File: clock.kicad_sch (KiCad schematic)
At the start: 10 parts

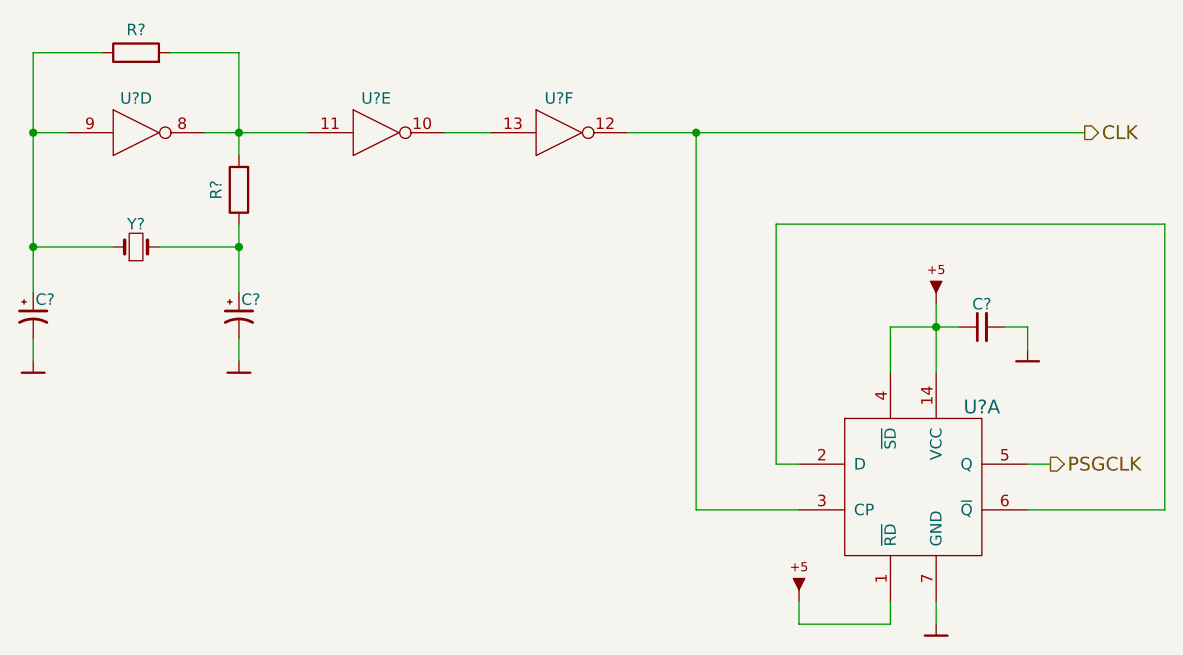
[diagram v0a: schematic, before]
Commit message: Fix wrong cap type in clock generator
Also fill some references automatically generated by KiCAD.
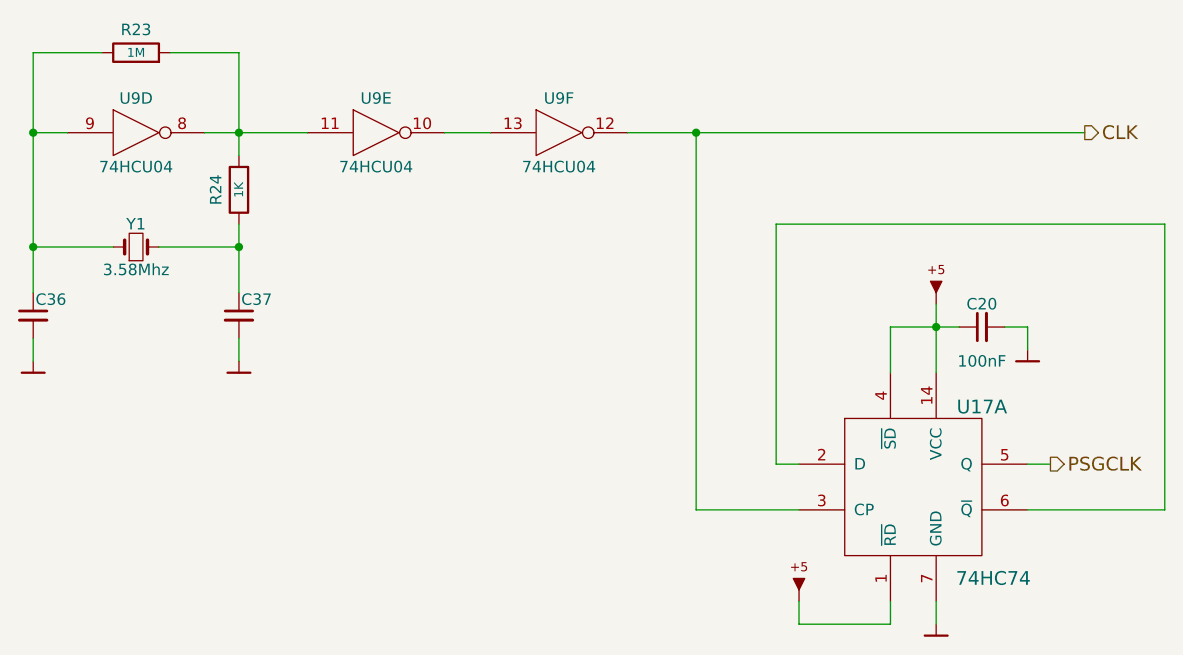
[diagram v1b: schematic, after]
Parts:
- C20: renamed from C?; value (none) -> 100nF; footprint (none) -> artemisa:Disc_capacitor
- C36, C37: renamed from C?; symbol artemisa:CP -> artemisa:Cap
- R23: renamed from R?; value (none) -> 1M; footprint (none) -> artemisa:Axial_resistor
- R24: renamed from R?; value (none) -> 1K; footprint (none) -> artemisa:Axial_resistor
- U17: renamed from U?; value (none) -> 74HC74; footprint (none) -> artemisa:DIP-14_300
- U9: renamed from U?; value (none) -> 74HCU04; footprint (none) -> artemisa:DIP-14_300
- Y1: renamed from Y?; value (none) -> 3.58Mhz; footprint (none) -> artemisa:Crystal
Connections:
- net VCC: now reaches U17.1 (~{RD})
- net VCC: now also C20.1, U17.14 (VCC), U17.4 (~{SD})
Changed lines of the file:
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@@
   (symbol (lib_id "artemisa:Crystal") (at 85.09 87.63 0) (unit 1)
     (in_bom yes) (on_board yes)
-    (property "Reference" "Y?" (id 0) (at 85.09 85.09 0))
-    (property "Value" "" (id 1) (at 85.09 90.17 0))
-    (property "Footprint" "" (id 2) (at 85.09 87.63 0)
+    (property "Reference" "Y1" (id 0) (at 85.09 85.09 0))
+    (property "Value" "3.58Mhz" (id 1) (at 85.09 90.17 0))
+    (property "Footprint" "artemisa:Crystal" (id 2) (at 85.09 87.63 0)
       (effects (font (size 1.27 1.27)) hide)
     )
@@
     (pin "2")
   )
-  (symbol (lib_id "artemisa:CP") (at 73.66 95.25 0) (unit 1)
-    (in_bom yes) (on_board yes)
-    (property "Reference" "C?" (id 0) (at 73.914 93.472 0)
+  (symbol (lib_id "artemisa:Cap") (at 73.66 95.25 0) (unit 1)
+    (in_bom yes) (on_board yes)
+    (property "Reference" "C36" (id 0) (at 73.914 93.472 0)
       (effects (font (size 1.27 1.27)) (justify left))
     )
@@
     (pin "2")
   )
-  (symbol (lib_id "artemisa:CP") (at 96.52 95.25 0) (unit 1)
-    (in_bom yes) (on_board yes)
-    (property "Reference" "C?" (id 0) (at 96.774 93.472 0)
+  (symbol (lib_id "artemisa:Cap") (at 96.52 95.25 0) (unit 1)
+    (in_bom yes) (on_board yes)
+    (property "Reference" "C37" (id 0) (at 96.774 93.472 0)
       (effects (font (size 1.27 1.27)) (justify left))
     )
@@
   (symbol (lib_id "artemisa:74HCU04") (at 85.09 74.93 0) (unit 4)
     (in_bom yes) (on_board yes)
-    (property "Reference" "U?" (id 0) (at 85.09 71.12 0))
-    (property "Value" "" (id 1) (at 85.09 78.74 0))
-    (property "Footprint" "" (id 2) (at 85.09 74.93 0)
+    (property "Reference" "U9" (id 0) (at 85.09 71.12 0))
+    (property "Value" "74HCU04" (id 1) (at 85.09 78.74 0))
+    (property "Footprint" "artemisa:DIP-14_300" (id 2) (at 85.09 74.93 0)
       (effects (font (size 1.27 1.27)) hide)
     )
@@
   (symbol (lib_id "artemisa:74HCU04") (at 111.76 74.93 0) (unit 5)
     (in_bom yes) (on_board yes)
-    (property "Reference" "U?" (id 0) (at 111.76 71.12 0))
-    (property "Value" "" (id 1) (at 111.76 78.74 0))
-    (property "Footprint" "" (id 2) (at 111.76 74.93 0)
+    (property "Reference" "U9" (id 0) (at 111.76 71.12 0))
+    (property "Value" "74HCU04" (id 1) (at 111.76 78.74 0))
+    (property "Footprint" "artemisa:DIP-14_300" (id 2) (at 111.76 74.93 0)
       (effects (font (size 1.27 1.27)) hide)
     )
@@
   (symbol (lib_id "artemisa:R") (at 96.52 81.28 90) (unit 1)
     (in_bom yes) (on_board yes)
-    (property "Reference" "R?" (id 0) (at 93.98 81.28 0))
-    (property "Value" "" (id 1) (at 96.52 81.28 0)
+    (property "Reference" "R24" (id 0) (at 93.98 81.28 0))
+    (property "Value" "1K" (id 1) (at 96.52 81.28 0)
       (effects (font (size 0.9906 0.9906)))
     )
-    (property "Footprint" "" (id 2) (at 96.52 83.058 90)
+    (property "Footprint" "artemisa:Axial_resistor" (id 2) (at 96.52 83.058 90)
       (effects (font (size 1.27 1.27)) hide)
     )
@@
   (symbol (lib_id "artemisa:R") (at 85.09 66.04 0) (unit 1)
     (in_bom yes) (on_board yes)
-    (property "Reference" "R?" (id 0) (at 85.09 63.5 0))
-    (property "Value" "" (id 1) (at 85.09 66.04 0)
+    (property "Reference" "R23" (id 0) (at 85.09 63.5 0))
+    (property "Value" "1M" (id 1) (at 85.09 66.04 0)
       (effects (font (size 0.9906 0.9906)))
     )
-    (property "Footprint" "" (id 2) (at 83.312 66.04 90)
+    (property "Footprint" "artemisa:Axial_resistor" (id 2) (at 83.312 66.04 90)
       (effects (font (size 1.27 1.27)) hide)
     )
@@
   (symbol (lib_id "artemisa:74HCU04") (at 132.08 74.93 0) (unit 6)
     (in_bom yes) (on_board yes)
-    (property "Reference" "U?" (id 0) (at 132.08 71.12 0))
-    (property "Value" "" (id 1) (at 132.08 78.74 0))
-    (property "Footprint" "" (id 2) (at 132.08 74.93 0)
+    (property "Reference" "U9" (id 0) (at 132.08 71.12 0))
+    (property "Value" "74HCU04" (id 1) (at 132.08 78.74 0))
+    (property "Footprint" "artemisa:DIP-14_300" (id 2) (at 132.08 74.93 0)
       (effects (font (size 1.27 1.27)) hide)
     )
@@
   (symbol (lib_id "artemisa:74HC74") (at 171.45 114.3 0) (unit 1)
     (in_bom yes) (on_board yes)
-    (property "Reference" "U?" (id 0) (at 179.07 105.41 0)
+    (property "Reference" "U17" (id 0) (at 179.07 105.41 0)
       (effects (font (size 1.524 1.524)))
     )
-    (property "Value" "" (id 1) (at 180.34 124.46 0)
+    (property "Value" "74HC74" (id 1) (at 180.34 124.46 0)
       (effects (font (size 1.524 1.524)))
     )
-    (property "Footprint" "" (id 2) (at 171.45 119.38 0)
+    (property "Footprint" "artemisa:DIP-14_300" (id 2) (at 171.45 119.38 0)
       (effects (font (size 1.524 1.524)) hide)
     )
@@
       (effects (font (size 1.524 1.524)) hide)
     )
-    (property "Value" "" (id 1) (at 173.99 87.63 0)
+    (property "Value" "VCC" (id 1) (at 173.99 87.63 0)
       (effects (font (size 1.524 1.524)) hide)
     )
@@
       (effects (font (size 1.524 1.524)) hide)
     )
-    (property "Value" "" (id 1) (at 96.52 97.79 0)
+    (property "Value" "GND" (id 1) (at 96.52 97.79 0)
       (effects (font (size 1.524 1.524)) hide)
     )
@@
       (effects (font (size 1.524 1.524)) hide)
     )
-    (property "Value" "" (id 1) (at 73.66 97.79 0)
+    (property "Value" "GND" (id 1) (at 73.66 97.79 0)
       (effects (font (size 1.524 1.524)) hide)
     )
@@
   (symbol (lib_id "artemisa:Cap") (at 179.07 96.52 90) (unit 1)
     (in_bom yes) (on_board yes)
-    (property "Reference" "C?" (id 0) (at 179.07 93.98 90))
-    (property "Value" "" (id 1) (at 179.07 100.33 90))
-    (property "Footprint" "" (id 2) (at 179.07 96.52 0)
+    (property "Reference" "C20" (id 0) (at 179.07 93.98 90))
+    (property "Value" "100nF" (id 1) (at 179.07 100.33 90))
+    (property "Footprint" "artemisa:Disc_capacitor" (id 2) (at 179.07 96.52 0)
       (effects (font (size 1.27 1.27)) hide)
     )
@@
       (effects (font (size 1.524 1.524)) hide)
     )
-    (property "Value" "" (id 1) (at 158.75 120.65 0)
+    (property "Value" "VCC" (id 1) (at 158.75 120.65 0)
       (effects (font (size 1.524 1.524)) hide)
     )
@@
       (effects (font (size 1.524 1.524)) hide)
     )
-    (property "Value" "" (id 1) (at 184.15 96.52 0)
+    (property "Value" "GND" (id 1) (at 184.15 96.52 0)
       (effects (font (size 1.524 1.524)) hide)
     )
@@
       (effects (font (size 1.524 1.524)) hide)
     )
-    (property "Value" "" (id 1) (at 173.99 127 0)
-      (effects (font (size 1.524 1.524)) hide)
-    )
+    (property "Value" "GND" (id 1) (at 173.99 127 0)
+      (effects (font (size 1.524 1.524)) hide)
+    )

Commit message: Upgrade project files to KiCad v8
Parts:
- C36, C37: value (none) -> 33pF; footprint (none) -> artemisa:Disc_capacitor
